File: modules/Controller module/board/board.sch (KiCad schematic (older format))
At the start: 31 parts, among them J1 USB_C_Receptacle, J2 Conn_01x05_Female, J3 Conn_01x03_Female, J4 Conn_01x04_Female, J5 Conn_02x12_Odd_Even, J6 Conn_01x06_Female, Q1 AO3400A, SW1 SW_Push, SW2 SW_Push, U1 HT7833, U2 ESP32-WROOM-32D

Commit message: Controller module: Schematic and PCB layout
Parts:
- removed C1, C3: 1nF, Capacitor_SMD:C_0805_2012Metric_Pad1.18x1.45mm_HandSolder, symbol Device:C_Small
- removed D2: LED_RGBC, LED_THT:LED_D5.0mm-4_RGB, symbol Device:LED_RGBC
- removed J1: USB_C_Receptacle, Connector_USB:USB_C_Receptacle_JAE_DX07S024WJ1R350, symbol Connector:USB_C_Receptacle
- removed J3: Conn_01x03_Female, Connector_PinSocket_2.54mm:PinSocket_1x03_P2.54mm_Vertical, symbol Connector:Conn_01x03_Female
- removed J5: Conn_02x12_Odd_Even, Connector_PinSocket_2.54mm:PinSocket_2x12_P2.54mm_Vertical_SMD, symbol Connector_Generic:Conn_02x12_Odd_Even
- removed U1: HT7833, Package_TO_SOT_SMD:SOT-89-3, symbol Regulator_Linear:HT75xx-1-SOT89
- added D2: LED_RGB, LED_SMD:LED_RGB_5050-6, symbol Device:LED_RGB
- added J2: Conn_01x04_Female, Board:SolderWire_1x04_P2.00mm, symbol Connector:Conn_01x04_Female
- added J4: Conn_01x02, Board:SolderWire_1x02_P2.00mm, symbol Connector_Generic:Conn_01x02
- added P1: USB_C_Plug_USB2.0, Board:GCT_USB4151-GF-C_REVA, symbol Connector:USB_C_Plug_USB2.0
- added Q2: AO3400A, Package_TO_SOT_SMD:SOT-23, symbol Transistor_FET:AO3400A
- added R1, R2, R5, R9: 10k, Resistor_SMD:R_0805_2012Metric_Pad1.20x1.40mm_HandSolder, symbol Device:R_Small_US
- added R4, R8: 100R, Resistor_SMD:R_0805_2012Metric_Pad1.20x1.40mm_HandSolder, symbol Device:R_Small_US
- added SW3: SW_SPST, Connector_PinSocket_2.54mm:PinSocket_1x03_P2.54mm_Vertical, symbol Switch:SW_SPST
- added U1: ME6211, Package_TO_SOT_SMD:SOT-23-5_HandSoldering, symbol ME6211:ME6211
- C1: renamed from C2; value 1uF -> 10uF
- C2: renamed from C4; value 2.2uF -> 10uF
- H1, H2, H3, H4: footprint MountingHole:MountingHole_3.2mm_M3 -> MountingHole:MountingHole_2.2mm_M2
- J1: renamed from J2; footprint Connector_PinSocket_2.54mm:PinSocket_1x05_P2.54mm_Vertical -> Board:SolderWire_1x05_P2.00mm
- J3: renamed from J4; footprint Connector_PinSocket_2.54mm:PinSocket_1x04_P2.54mm_Vertical -> Board:SolderWire_1x04_P2.00mm
- J5: renamed from J6; footprint Connector_PinSocket_2.54mm:PinSocket_1x06_P2.54mm_Vertical -> Board:SolderWire_1x06_P2.54mm
- SW1, SW2: footprint Button_Switch_SMD:SW_SPST_Omron_B3FS-100xP -> Button_Switch_SMD:SW_SPST_B3U-1000P
- renumbered R4 to R10, R18 to R11, R19 to R12, R5 to R13, R6 to R14, R7 to R15, R1 to R3, R2 to R6, R3 to R7
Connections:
- net labels added: BTN-C, VIBRATOR
- wire segments 138 -> 141
- no-connect marks 26 -> 14
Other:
- note removed: "Vibrator motor"
- moved on the sheet: BZ1, C1, C2, D1, H1, H2, H3, H4, J1, J3, J5, Q1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

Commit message: Controller module: PCB complete
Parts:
- added D2: LED, LED_SMD:LED_0805_2012Metric_Pad1.15x1.40mm_HandSolder, symbol Device:LED
- added R6: 10k, Resistor_SMD:R_0805_2012Metric_Pad1.20x1.40mm_HandSolder, symbol Device:R_Small_US
- U2: footprint RF_Module:ESP32-WROOM-32 -> Board:ESP32-WROOM-32
- renumbered D2 to D3, R9 to R10, R10 to R11, R11 to R12, R12 to R13, R13 to R14, R14 to R15, R15 to R16, R6 to R7, R7 to R8, R8 to R9, SW3 to SW2, SW2 to SW3
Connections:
- net IO5 is gone; now on net IO15: U2.29 (IO5)
- net GND: now also D2.1 (K)
- net IO15: now also R6.1
- new net: D2.2 (A), R6.2
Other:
- moved on the sheet: C1, C2, R11, R7, R8, SW1, SW2, SW3, U1

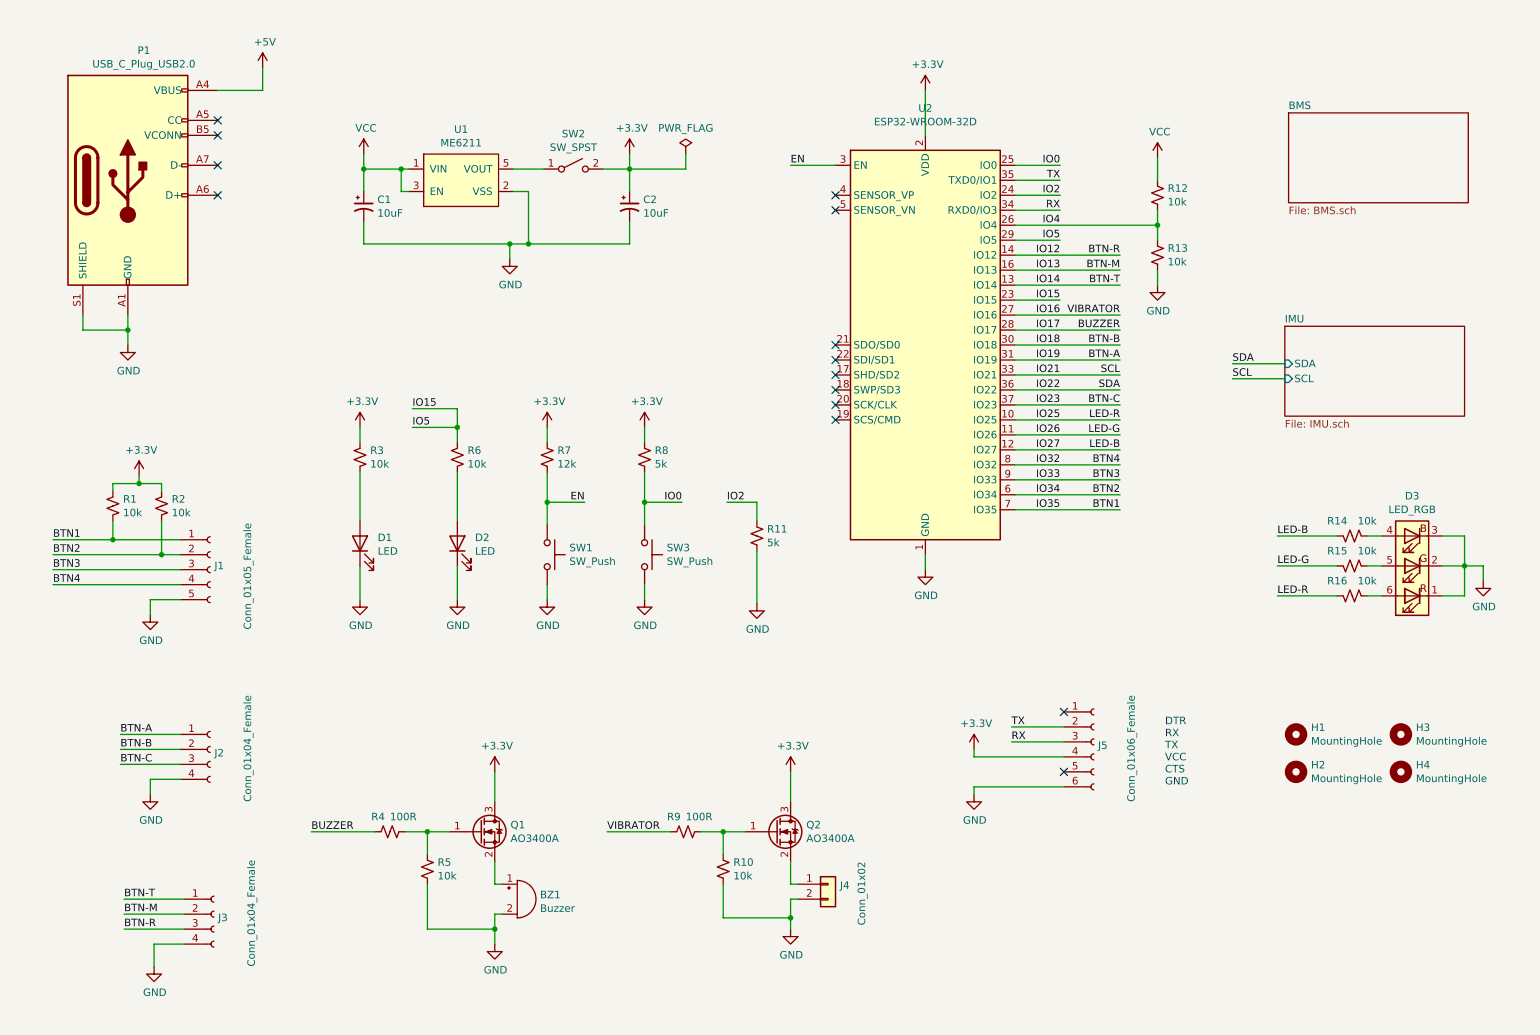
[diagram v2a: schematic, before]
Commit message: Controller module: PCB modular
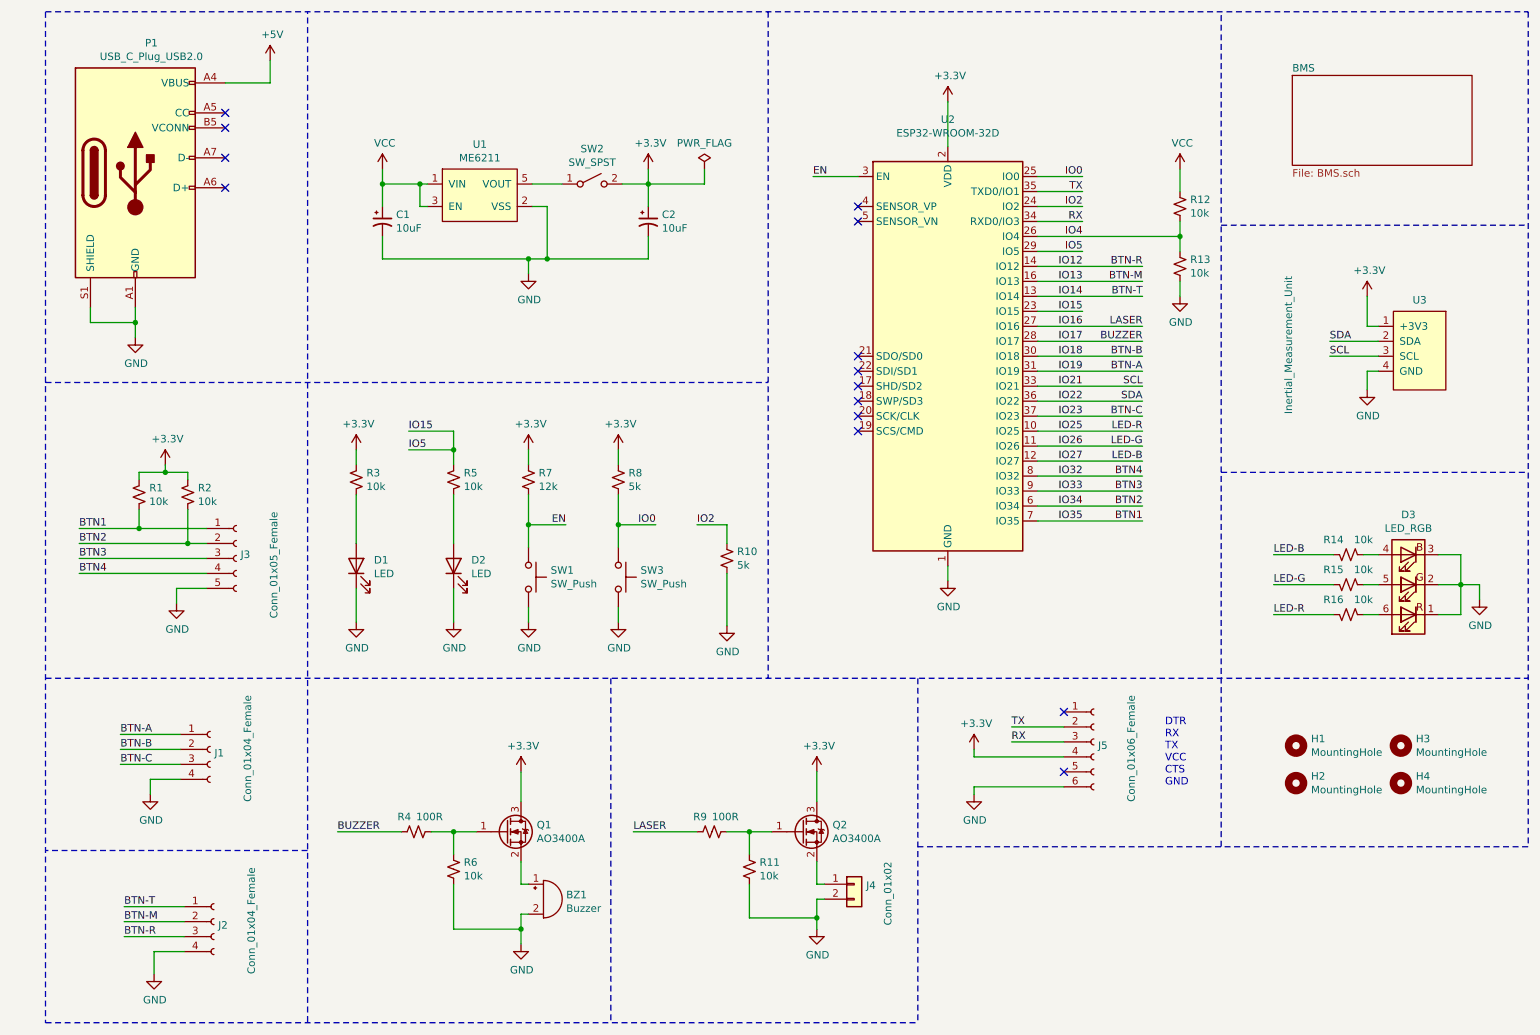
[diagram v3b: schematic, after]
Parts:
- added U3: Inertial_Measurement_Unit, Board:Inertial_Measurement_Unit_Board, symbol Board:Inertial_Measurement_Unit
- renumbered J2 to J1, J3 to J2, J1 to J3, R11 to R10, R10 to R11, R6 to R5, R5 to R6
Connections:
- net +3V3: now also U3.1 (+3V3)
- net GND: now also U3.4 (GND)
- net IO21: now also U3.3 (SCL)
- net IO22: now also U3.2 (SDA)
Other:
- moved on the sheet: BZ1, C1, C2, D1, D2, D3, H1, H2, H3, H4, J2, J3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

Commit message: PCB: IMU
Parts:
- removed D2: LED, LED_SMD:LED_0805_2012Metric_Pad1.15x1.40mm_HandSolder, symbol Device:LED
- removed R5: 10k, Resistor_SMD:R_0805_2012Metric_Pad1.20x1.40mm_HandSolder, symbol Device:R_Small_US
- removed U3: Inertial_Measurement_Unit, Board:Inertial_Measurement_Unit_Board, symbol Board:Inertial_Measurement_Unit
- renumbered D3 to D2, R11 to R10, R12 to R11, R13 to R12, R14 to R13, R15 to R14, R16 to R15, R6 to R5, R7 to R6, R8 to R7, R10 to R8
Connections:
- net BTN-A: now also U2.28 (IO17); no longer U2.31 (IO19)
- net BTN-B: now also U2.27 (IO16); no longer U2.30 (IO18)
- net BTN-M: now also U2.14 (IO12); no longer U2.16 (IO13)
- net BTN-T: now also U2.16 (IO13); no longer U2.13 (IO14)
- net BUZZER: now also U2.23 (IO15); no longer U2.28 (IO17)
- net BTN-R renamed BTN-S
- net BTN-S: now also U2.29 (IO5); no longer U2.14 (IO12)
- removed net IO15: U2.23 (IO15), U2.29 (IO5)
- net IO16 renamed IO14
- net IO14: now also U2.13 (IO14); no longer U2.27 (IO16)
- net IO21 renamed SCL
- net IO22 renamed SDA
- new net INT1: U2.30 (IO18)
- new net INT2: U2.31 (IO19)
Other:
- moved on the sheet: R11, R12, R6, R7, R8, SW1, SW3, U2

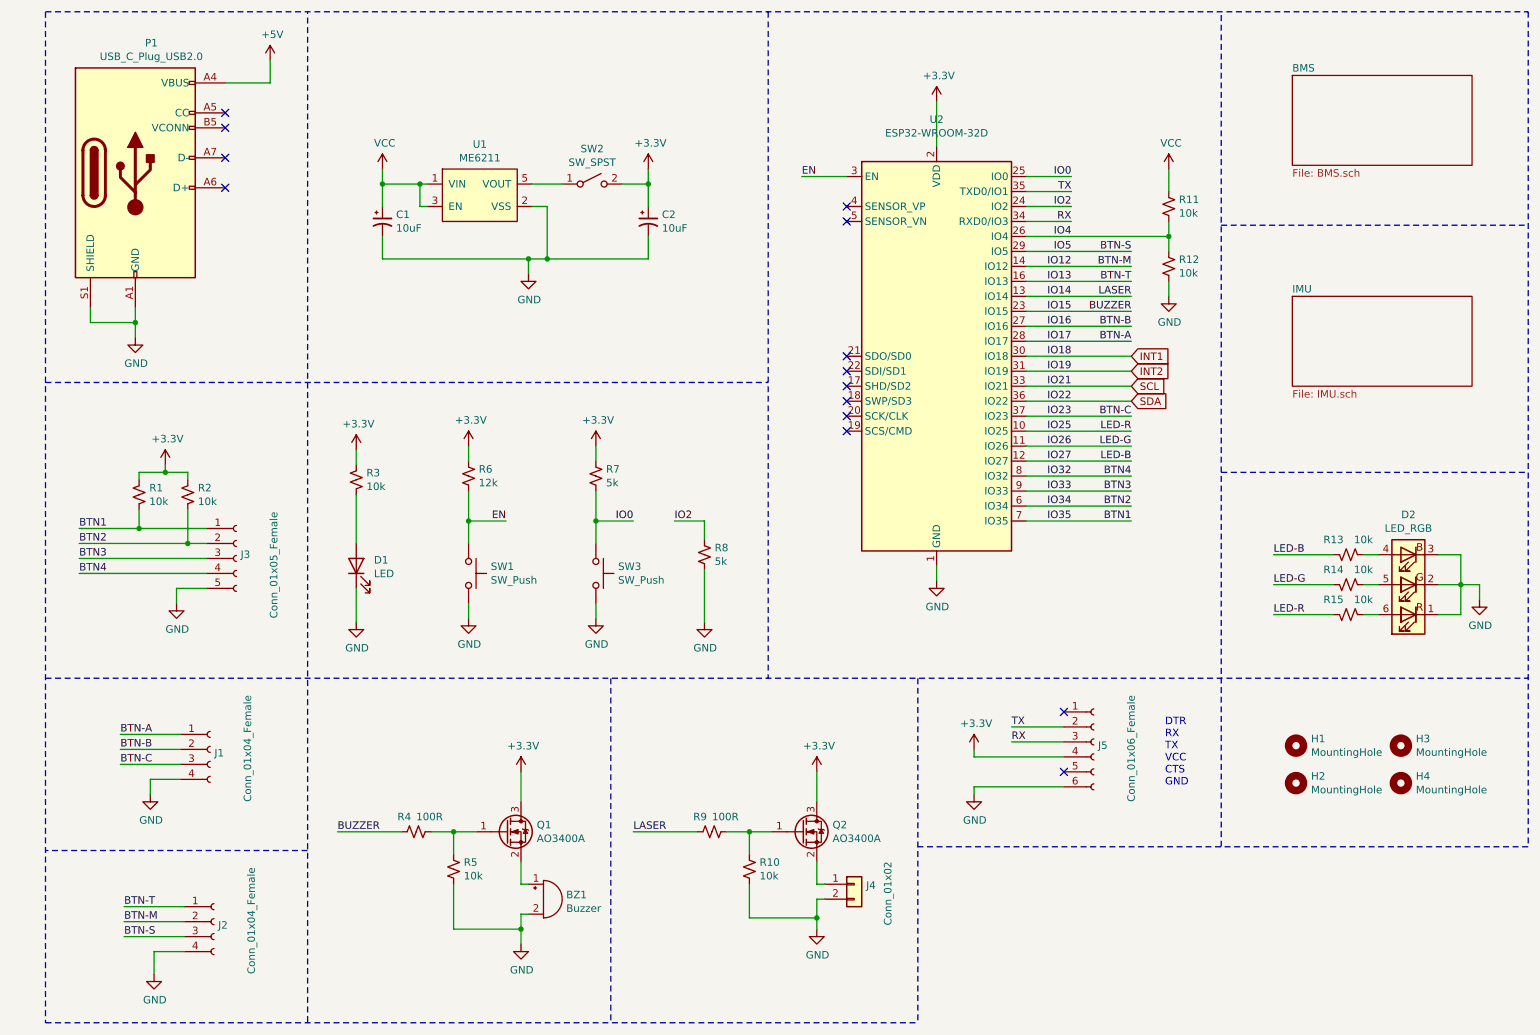
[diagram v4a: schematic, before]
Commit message: Controller module: Optical Flow Sensor Connector
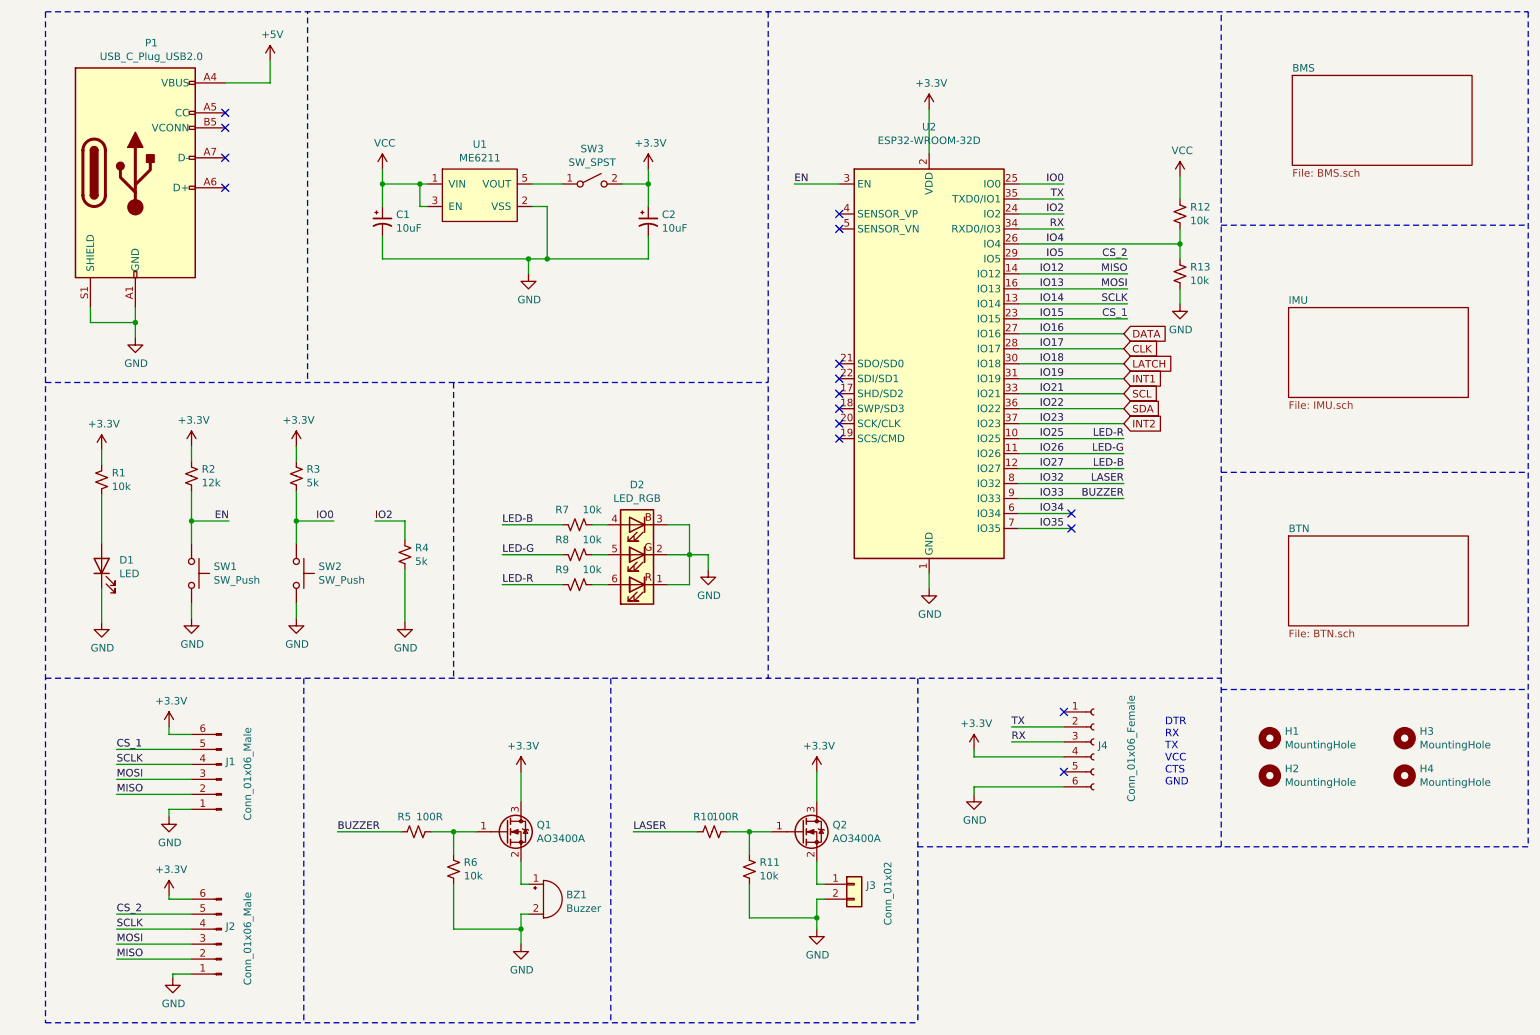
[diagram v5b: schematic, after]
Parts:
- removed J1, J2: Conn_01x04_Female, Board:SolderWire_1x04_P2.00mm, symbol Connector:Conn_01x04_Female
- removed J3: Conn_01x05_Female, Board:SolderWire_1x05_P2.00mm, symbol Connector:Conn_01x05_Female
- removed R1, R2: 10k, Resistor_SMD:R_0805_2012Metric_Pad1.20x1.40mm_HandSolder, symbol Device:R_Small_US
- added J1, J2: Conn_01x06_Male, Board:SolderWire_1x06_P2.54mm, symbol Connector:Conn_01x06_Male
- SW3: renamed from SW2; footprint Connector_PinSocket_2.54mm:PinSocket_1x03_P2.54mm_Vertical -> Board:SolderWire_1x02_P2.00mm
- renumbered J4 to J3, J5 to J4, R3 to R1, R9 to R10, R10 to R11, R11 to R12, R12 to R13, R6 to R2, R7 to R3, R8 to R4, R4 to R5, R5 to R6, R13 to R7, R14 to R8, R15 to R9, SW3 to SW2
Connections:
- net BTN-C is gone; now on net INT2: U2.37 (IO23)
- net BTN3 is gone; now on net BUZZER: U2.9 (IO33)
- net +3V3: now also J1.6 (Pin_6), J2.6 (Pin_6)
- net BUZZER: no longer U2.23 (IO15)
- net GND: now also J1.1 (Pin_1), J2.1 (Pin_1)
- net INT1: now also U2.31 (IO19); no longer U2.30 (IO18)
- net INT2: no longer U2.31 (IO19)
- net IO14: now also J1.4 (Pin_4), J2.4 (Pin_4); no longer R10.2
- net BTN-A renamed CLK
- net BTN-B renamed DATA
- net BTN-M renamed IO12
- net IO12: now also J1.2 (Pin_2), J2.2 (Pin_2)
- net BTN-S renamed CS_2
- net CS_2: now also J2.5 (Pin_5)
- net BTN-T renamed IO13
- net IO13: now also J1.3 (Pin_3), J2.3 (Pin_3)
- net BTN1 renamed IO35
- net BTN2 renamed IO34
- net BTN4 renamed IO32
- net IO32: now also R10.2
- new net CS_1: J1.5 (Pin_5), U2.23 (IO15)
- new net LATCH: U2.30 (IO18)
- no-connect marks 14 -> 16
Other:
- moved on the sheet: D1, D2, H1, H2, H3, H4, R1, R12, R13, R2, R3, R4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
